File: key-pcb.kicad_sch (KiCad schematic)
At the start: 24 parts, among them J1 row left, J10 DIN bottom, J11 DOUT bottom, J12 VDD bottom, J13 VSS left, J14 DOUT left, J15 DIN left, J16 VDD left, J17 VDD right, J18 DOUT right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

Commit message: First attempt at layout. Not good.
Pins are too close together and won't fit on board.
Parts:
- C1: footprint (none) -> Capacitor_SMD:C_0805_2012Metric_Pad1.18x1.45mm_HandSolder
- J1, J10, J11, J12, J13, J14, J15, J16, J17, J18, J19, J2, J20, J3, J4, J5, J6, J7, J8, J9: footprint (none) -> Connector_PinHeader_2.54mm:PinHeader_1x01_P2.54mm_Vertical
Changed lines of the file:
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@@
 			)
 		)
-		(property "Footprint" ""
+		(property "Footprint" "Connector_PinHeader_2.54mm:PinHeader_1x01_P2.54mm_Vertical"
 			(at 177.8 38.1 0)
 			(effects
@@
 			)
 		)
-		(property "Footprint" ""
+		(property "Footprint" "Connector_PinHeader_2.54mm:PinHeader_1x01_P2.54mm_Vertical"
 			(at 203.2 106.68 0)
 			(effects
@@
 			)
 		)
-		(property "Footprint" ""
+		(property "Footprint" "Connector_PinHeader_2.54mm:PinHeader_1x01_P2.54mm_Vertical"
 			(at 58.42 88.9 0)
 			(effects
@@
 			)
 		)
-		(property "Footprint" ""
+		(property "Footprint" "Connector_PinHeader_2.54mm:PinHeader_1x01_P2.54mm_Vertical"
 			(at 142.24 88.9 0)
 			(effects
@@
 			)
 		)
-		(property "Footprint" ""
+		(property "Footprint" "Connector_PinHeader_2.54mm:PinHeader_1x01_P2.54mm_Vertical"
 			(at 220.98 63.5 0)
 			(effects
@@
 			)
 		)
-		(property "Footprint" ""
+		(property "Footprint" "Connector_PinHeader_2.54mm:PinHeader_1x01_P2.54mm_Vertical"
 			(at 203.2 38.1 0)
 			(effects
@@
 			)
 		)
-		(property "Footprint" ""
+		(property "Footprint" "Connector_PinHeader_2.54mm:PinHeader_1x01_P2.54mm_Vertical"
 			(at 220.98 50.8 0)
 			(effects
@@
 			)
 		)
-		(property "Footprint" ""
+		(property "Footprint" "Connector_PinHeader_2.54mm:PinHeader_1x01_P2.54mm_Vertical"
 			(at 177.8 106.68 0)
 			(effects
@@
 			)
 		)
-		(property "Footprint" ""
+		(property "Footprint" "Connector_PinHeader_2.54mm:PinHeader_1x01_P2.54mm_Vertical"
 			(at 165.1 38.1 0)
 			(effects
@@
 			)
 		)
-		(property "Footprint" ""
+		(property "Footprint" "Connector_PinHeader_2.54mm:PinHeader_1x01_P2.54mm_Vertical"
 			(at 93.98 88.9 0)
 			(effects
@@
 			)
 		)
-		(property "Footprint" ""
+		(property "Footprint" "Connector_PinHeader_2.54mm:PinHeader_1x01_P2.54mm_Vertical"
 			(at 220.98 76.2 0)
 			(effects
@@
 			)
 		)
-		(property "Footprint" ""
+		(property "Footprint" "Connector_PinHeader_2.54mm:PinHeader_1x01_P2.54mm_Vertical"
 			(at 220.98 88.9 0)
 			(effects
@@
 			)
 		)
-		(property "Footprint" ""
+		(property "Footprint" "Connector_PinHeader_2.54mm:PinHeader_1x01_P2.54mm_Vertical"
 			(at 107.95 106.68 0)
 			(effects
@@
 			)
 		)
-		(property "Footprint" ""
+		(property "Footprint" "Capacitor_SMD:C_0805_2012Metric_Pad1.18x1.45mm_HandSolder"
 			(at 175.26 58.7248 0)
 			(effects
@@
 			)
 		)
-		(property "Footprint" ""
+		(property "Footprint" "Connector_PinHeader_2.54mm:PinHeader_1x01_P2.54mm_Vertical"
 			(at 142.24 76.2 0)
 			(effects
@@
 			)
 		)
-		(property "Footprint" ""
+		(property "Footprint" "Connector_PinHeader_2.54mm:PinHeader_1x01_P2.54mm_Vertical"
 			(at 190.5 38.1 0)
 			(effects
@@
 			)
 		)
-		(property "Footprint" ""
+		(property "Footprint" "Connector_PinHeader_2.54mm:PinHeader_1x01_P2.54mm_Vertical"
 			(at 107.95 45.72 0)
 			(effects
@@
 			)
 		)
-		(property "Footprint" ""
+		(property "Footprint" "Connector_PinHeader_2.54mm:PinHeader_1x01_P2.54mm_Vertical"
 			(at 190.5 106.68 0)
 			(effects
@@
 			)
 		)
-		(property "Footprint" ""
+		(property "Footprint" "Connector_PinHeader_2.54mm:PinHeader_1x01_P2.54mm_Vertical"
 			(at 142.24 63.5 0)
 			(effects
@@
 			)
 		)
-		(property "Footprint" ""
+		(property "Footprint" "Connector_PinHeader_2.54mm:PinHeader_1x01_P2.54mm_Vertical"
 			(at 142.24 50.8 0)
 			(effects
@@
 			)
 		)
-		(property "Footprint" ""
+		(property "Footprint" "Connector_PinHeader_2.54mm:PinHeader_1x01_P2.54mm_Vertical"
 			(at 165.1 106.68 0)
 			(effects

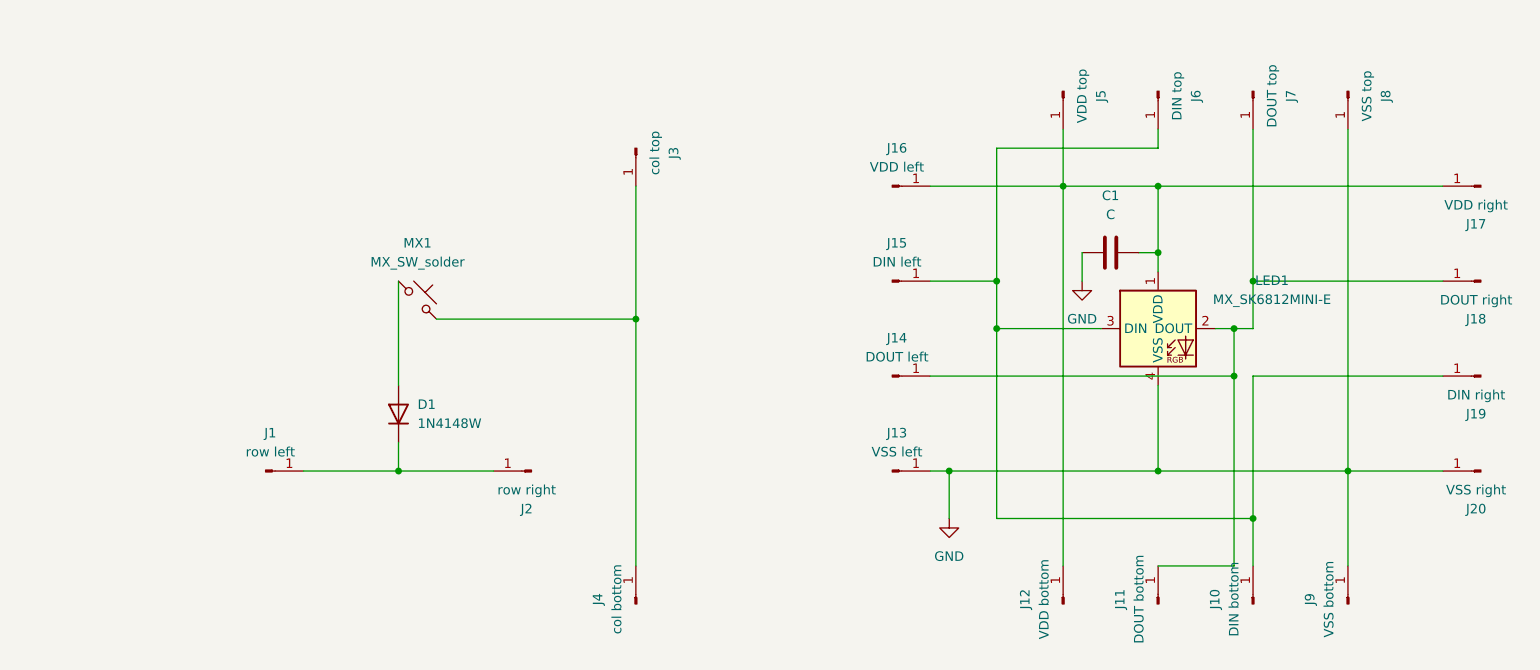
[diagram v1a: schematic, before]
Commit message: Routed, but DRC violation
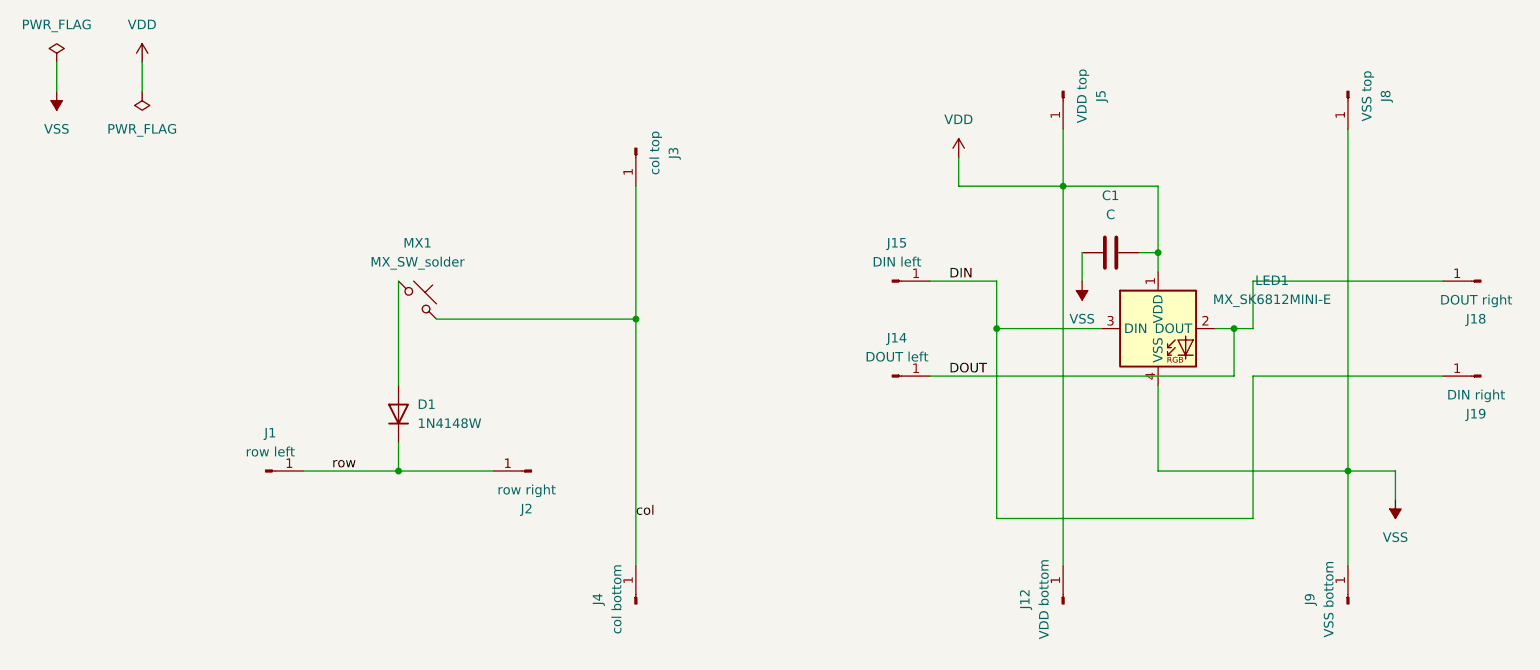
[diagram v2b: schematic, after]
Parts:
- removed J10: DIN bottom, Connector_PinHeader_2.54mm:PinHeader_1x01_P2.54mm_Vertical, symbol Connector:Conn_01x01_Pin
- removed J11: DOUT bottom, Connector_PinHeader_2.54mm:PinHeader_1x01_P2.54mm_Vertical, symbol Connector:Conn_01x01_Pin
- removed J13: VSS left, Connector_PinHeader_2.54mm:PinHeader_1x01_P2.54mm_Vertical, symbol Connector:Conn_01x01_Pin
- removed J16: VDD left, Connector_PinHeader_2.54mm:PinHeader_1x01_P2.54mm_Vertical, symbol Connector:Conn_01x01_Pin
- removed J17: VDD right, Connector_PinHeader_2.54mm:PinHeader_1x01_P2.54mm_Vertical, symbol Connector:Conn_01x01_Pin
- removed J20: VSS right, Connector_PinHeader_2.54mm:PinHeader_1x01_P2.54mm_Vertical, symbol Connector:Conn_01x01_Pin
- removed J6: DIN top, Connector_PinHeader_2.54mm:PinHeader_1x01_P2.54mm_Vertical, symbol Connector:Conn_01x01_Pin
- removed J7: DOUT top, Connector_PinHeader_2.54mm:PinHeader_1x01_P2.54mm_Vertical, symbol Connector:Conn_01x01_Pin
- C1: footprint Capacitor_SMD:C_0805_2012Metric_Pad1.18x1.45mm_HandSolder -> Capacitor_SMD:C_0603_1608Metric_Pad1.08x0.95mm_HandSolder
- J1, J12, J14, J15, J18, J19, J2, J3, J4, J5, J8, J9: footprint Connector_PinHeader_2.54mm:PinHeader_1x01_P2.54mm_Vertical -> TestPoint:TestPoint_Pad_1.0x1.0mm
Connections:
- net row: now reaches D1.1 (K), J1.1 (Pin_1), J2.1 (Pin_1)
- net DIN: now reaches J15.1 (Pin_1), J19.1 (Pin_1), LED1.3 (DIN)
- net DOUT: now reaches J14.1 (Pin_1), J18.1 (Pin_1), LED1.2 (DOUT)
- net VDD: now reaches C1.2, J12.1 (Pin_1), J5.1 (Pin_1), LED1.1 (VDD)
- net col: now reaches J3.1 (Pin_1), J4.1 (Pin_1), MX1.2
- net GND renamed VSS
